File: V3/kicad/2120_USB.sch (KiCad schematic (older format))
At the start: 6 parts, among them J2120 USB_B, J2122 Conn_01x02_Male, U2120 MCP2221AxP

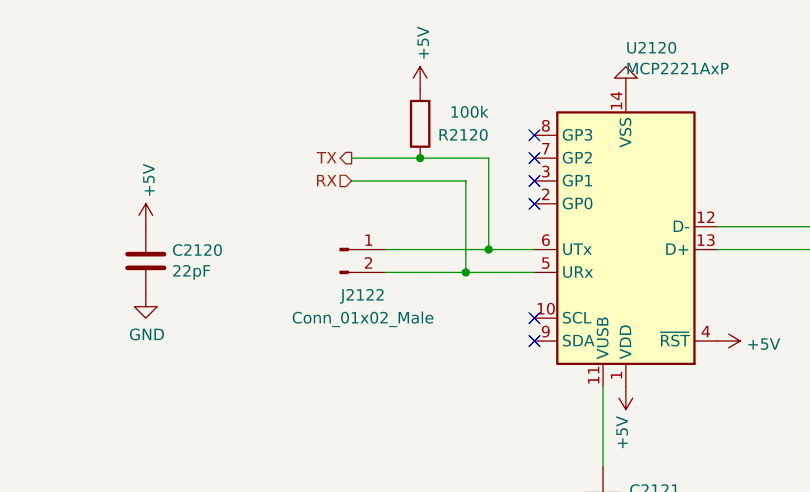
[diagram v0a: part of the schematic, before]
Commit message: new board layout, not routing yet, still need to check schematics
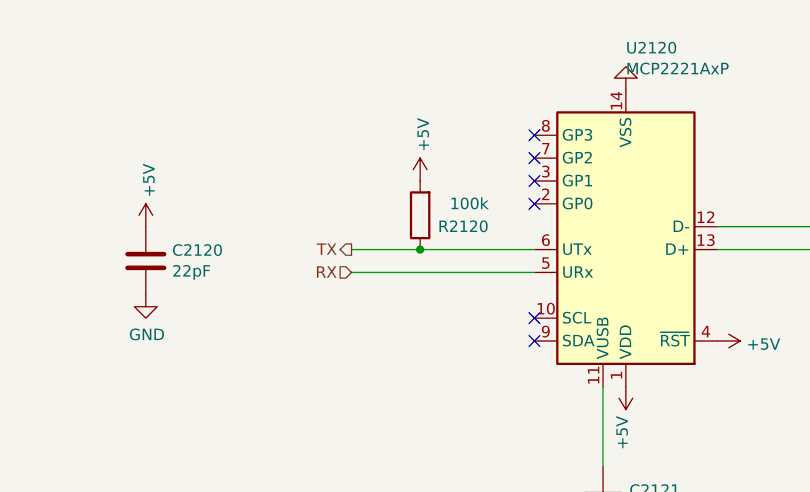
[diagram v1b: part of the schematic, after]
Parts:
- removed J2122: Conn_01x02_Male, Connector_PinHeader_2.54mm:PinHeader_1x02_P2.54mm_Vertical, symbol Connector:Conn_01x02_Male
- U2120: footprint Package_SO:SOIC-14_3.9x8.7mm_P1.27mm -> Package_DIP:DIP-14_W7.62mm_Socket_LongPads
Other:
- moved on the sheet: R2120
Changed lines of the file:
@@
 F 0 "U2120" H 5050 3119 50  0000 R CNN
 F 1 "MCP2221AxP" H 5050 3210 50  0000 R CNN
-F 2 "Package_SO:SOIC-14_3.9x8.7mm_P1.27mm" H 5050 4900 50  0001 C CNN
+F 2 "Package_DIP:DIP-14_W7.62mm_Socket_LongPads" H 5050 4900 50  0001 C CNN
 F 3 "http://ww1.microchip.com/downloads/en/DeviceDoc/20005565B.pdf" H 5050 4600 50  0001 C CNN
 	1    5050 3900
@@
 $EndComp
 $Comp
-L Connector:Conn_01x02_Male J2122
-U 1 1 627627D6
-P 3800 4000
-F 0 "J2122" H 3900 3800 50  0000 C CNN
-F 1 "Conn_01x02_Male" H 3900 3700 50  0000 C CNN
-F 2 "Connector_PinHeader_2.54mm:PinHeader_1x02_P2.54mm_Vertical" H 3800 4000 50  0001 C CNN
-F 3 "~" H 3800 4000 50  0001 C CNN
-	1    3800 4000
-	1    0    0    -1
-$EndComp
-Wire Wire Line
-	3850 3600 4150 3600
-Wire Wire Line
-	3850 3700 4350 3700
-$Comp
 L power:+5V #PWR?
 U 1 1 6278A36E
-P 4150 3300
+P 4150 3700
 AR Path="/6191B6A2/61EBDADB/6278A36E" Ref="#PWR?"  Part="1"
 AR Path="/6191B6A2/61EBDADB/62542978/6278A36E" Ref="#PWR0145"  Part="1"
 AR Path="/63A83936/62542978/6278A36E" Ref="#PWR0145"  Part="1"
-F 0 "#PWR0145" H 4150 3150 50  0001 C CNN
-F 1 "+5V" V 4165 3428 50  0000 L CNN
-F 2 "" H 4150 3300 50  0001 C CNN
-F 3 "" H 4150 3300 50  0001 C CNN
-	1    4150 3300
+F 0 "#PWR0145" H 4150 3550 50  0001 C CNN
+F 1 "+5V" V 4165 3828 50  0000 L CNN
+F 2 "" H 4150 3700 50  0001 C CNN
+F 3 "" H 4150 3700 50  0001 C CNN
+	1    4150 3700
 	1    0    0    -1
 $EndComp
@@
 L Device:R R2120
 U 1 1 6278730B
-P 4150 3450
-F 0 "R2120" H 3850 3500 50  0000 L CNN
-F 1 "100k" H 3850 3400 50  0000 L CNN
-F 2 "Resistor_SMD:R_1206_3216Metric" V 4080 3450 50  0001 C CNN
-F 3 "~" H 4150 3450 50  0001 C CNN
-	1    4150 3450
-	-1   0    0    1
-$EndComp
-Wire Wire Line
-	4450 3600 4450 4000
-Wire Wire Line
-	4450 4000 4650 4000
-Connection ~ 4450 4000
-Wire Wire Line
-	4450 4000 4000 4000
-Wire Wire Line
-	4650 4100 4350 4100
-Wire Wire Line
-	4000 4100 4350 4100
-Connection ~ 4350 4100
-Wire Wire Line
-	4350 3700 4350 4100
-Text HLabel 3850 3600 0    50   Output ~ 0
-TX
-Text HLabel 3850 3700 0    50   Input ~ 0
-RX
-Connection ~ 4150 3600
-Wire Wire Line
-	4150 3600 4450 3600
+P 4150 3850
+F 0 "R2120" H 3850 3900 50  0000 L CNN
+F 1 "100k" H 3850 3800 50  0000 L CNN
+F 2 "Resistor_SMD:R_1206_3216Metric" V 4080 3850 50  0001 C CNN
+F 3 "~" H 4150 3850 50  0001 C CNN
+	1    4150 3850
+	-1   0    0    1
+$EndComp
 NoConn ~ 4650 3500
 NoConn ~ 4650 3600
 NoConn ~ 4650 3700
 NoConn ~ 4650 3800
+Connection ~ 4150 4000
+Text HLabel 3850 4100 0    50   Input ~ 0
+RX
+Text HLabel 3850 4000 0    50   Output ~ 0
+TX
+Wire Wire Line
+	3850 4000 4150 4000
+Wire Wire Line
+	3850 4100 4650 4100
+Wire Wire Line
+	4150 4000 4650 4000
 $EndSCHEMATC
